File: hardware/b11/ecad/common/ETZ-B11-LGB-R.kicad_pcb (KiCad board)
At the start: 2 copper layers, 29 x 88.8 mm, 0 parts

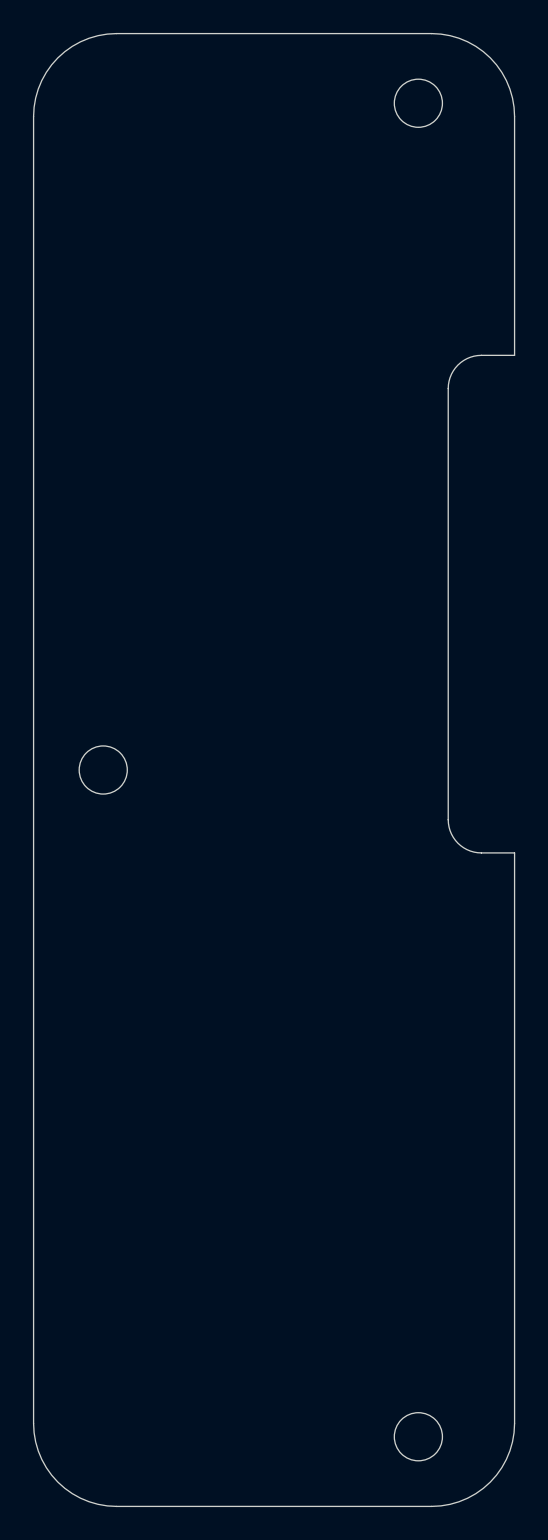
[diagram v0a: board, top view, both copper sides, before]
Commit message: feat: add logic board connector placement
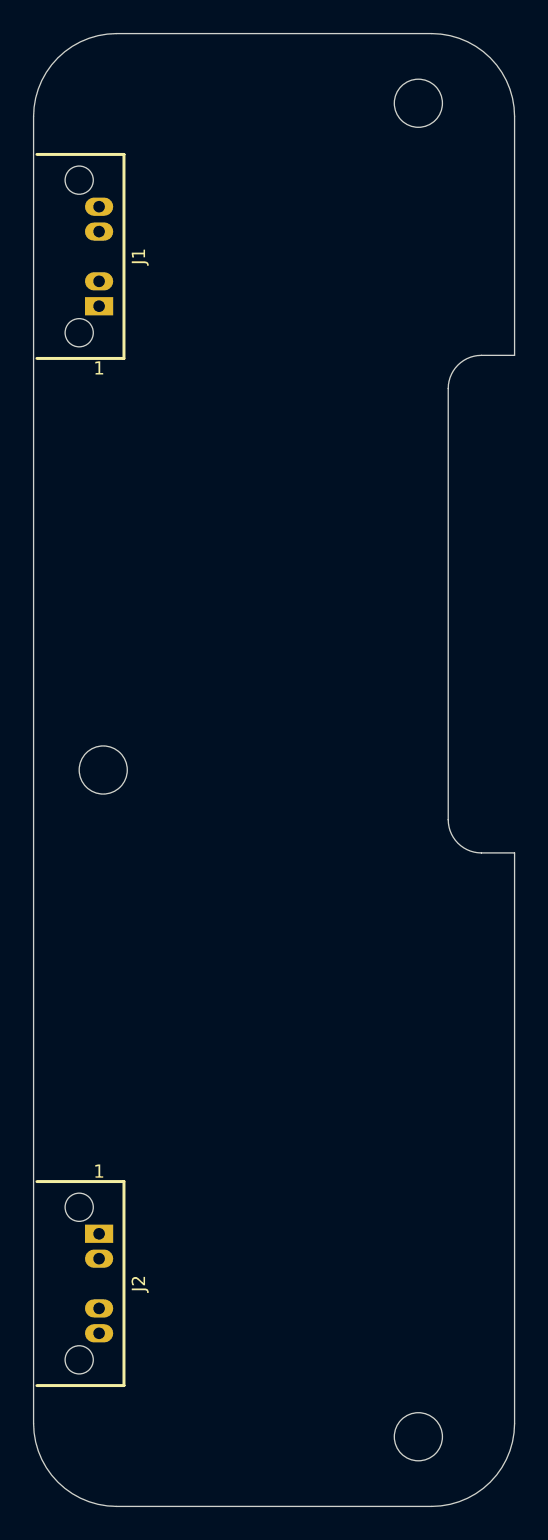
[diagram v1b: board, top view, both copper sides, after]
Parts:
- added J1: CN-HY04C-01D-FEMALE, CN-HY04C-01D-FEMALE, F.Cu at (134.0, 74.0)
- added J2: CN-HY04C-01D-MALE, CN-HY04C-01D-MALE, F.Cu at (134.0, 136.0)
